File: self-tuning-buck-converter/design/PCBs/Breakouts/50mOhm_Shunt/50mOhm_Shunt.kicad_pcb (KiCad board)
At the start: 2 copper layers, 15.2 x 7.6 mm, 5 parts, among them J1 Input +, J2 Kelvin +, J3 Input -, J4 Kelvin -

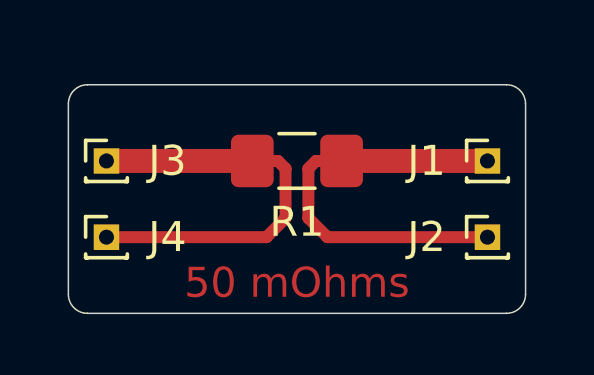
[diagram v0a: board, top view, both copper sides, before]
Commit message: update breakout PCB's for the 50mO and 60mO resistors. Ordered the missing parts
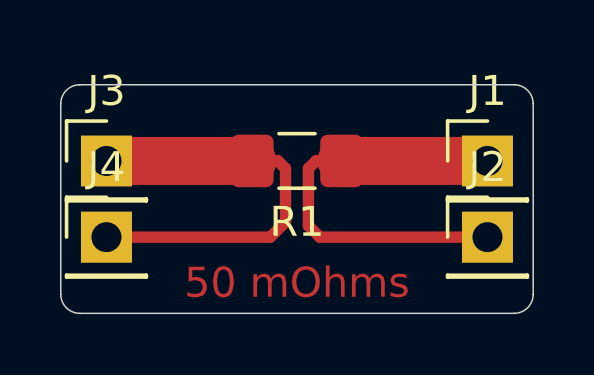
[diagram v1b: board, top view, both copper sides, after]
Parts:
- J1, J2, J3, J4: footprint Connector_PinHeader_1.00mm:PinHeader_1x01_P1.00mm_Vertical -> Connector_PinHeader_2.54mm:PinHeader_1x01_P2.54mm_Vertical
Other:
- board size 15.2 x 7.6 mm -> 15.7 x 7.6 mm
- net class Default: clearance 0.2 -> 0.381; trace_width 0.25 -> 0.381; via_drill 0.4 -> 0.6
- rule trace_clearance: 0.2 -> 0.381
- rule trace_min: 0.2 -> 0.381
- rule via_min_drill: 0.3 -> 0.6
- rule via_min_size: 0.4 -> 0.8

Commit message: updated breakout PCB's
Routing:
- net Net-(J3-Pad1): track 14.0 -> 9.17 mm
- net Net-(J1-Pad1): track 14.1 -> 9.24 mm
- added copper zone on F.Cu, net Net-(J1-Pad1)
- added copper zone on F.Cu, net Net-(J3-Pad1)
